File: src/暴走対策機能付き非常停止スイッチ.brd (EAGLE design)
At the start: 14 parts, among them T2 一般的なトランジスタ

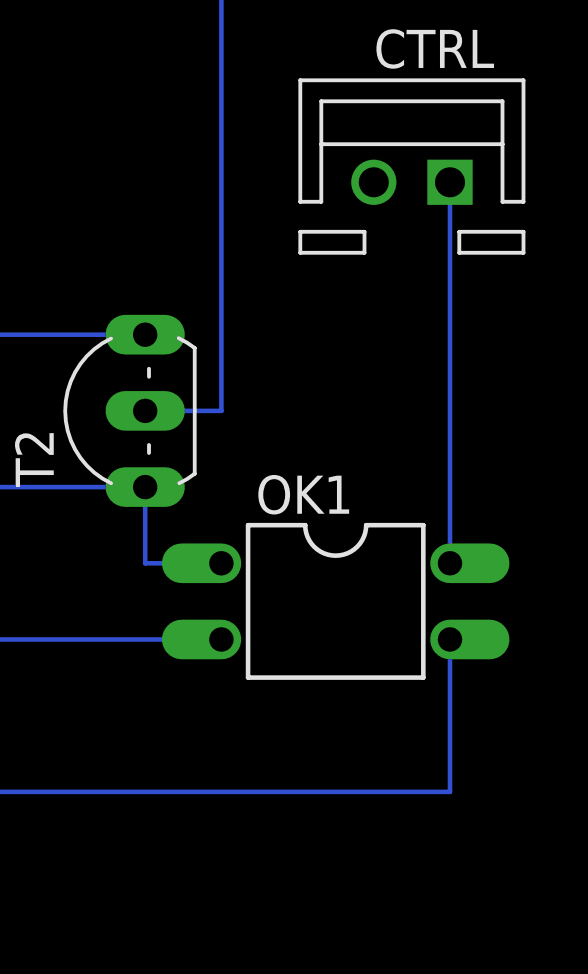
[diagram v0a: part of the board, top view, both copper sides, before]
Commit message: 暴走対策機能付き非常停止スイッチの回路のガバを修復
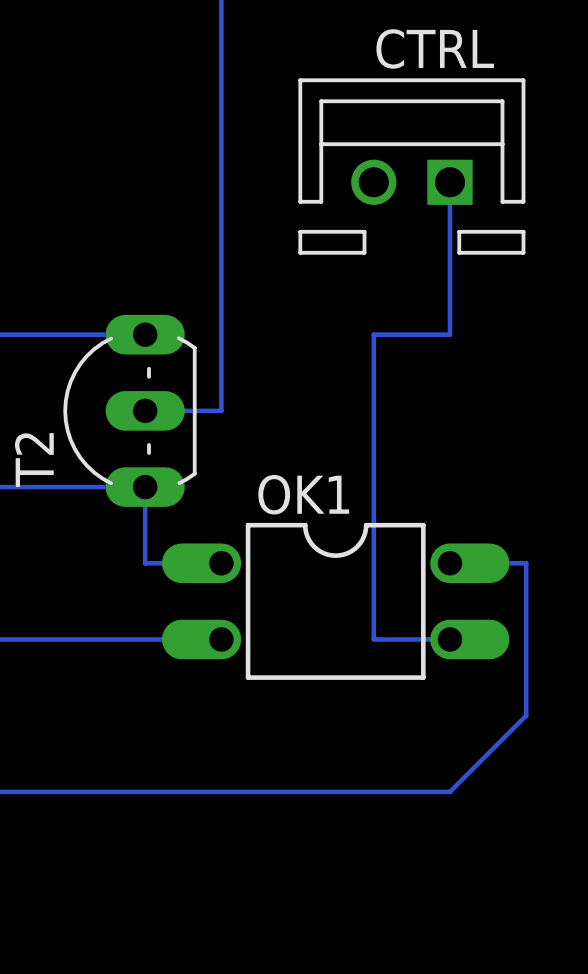
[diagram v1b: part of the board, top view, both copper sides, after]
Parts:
- R5: value 100k -> 10k
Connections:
- net GND2: now also OK1.3; no longer OK1.4
- net N$8: now also OK1.4; no longer OK1.3
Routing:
- net GND2: track 12.7 -> 20.3 mm
- net N$8: track 71.1 -> 77.3 mm
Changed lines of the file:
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@@
 <attribute name="VALUE" x="43.5356" y="20.8026" size="0.9906" layer="27" ratio="10" rot="R180"/>
 </element>
-<element name="R5" library="rcl" library_urn="urn:adsk.eagle:library:334" package="0204/7" package3d_urn="urn:adsk.eagle:package:23498/2" value="100k" x="16.51" y="10.16" smashed="yes">
+<element name="R5" library="rcl" library_urn="urn:adsk.eagle:library:334" package="0204/7" package3d_urn="urn:adsk.eagle:package:23498/2" value="10k" x="16.51" y="10.16" smashed="yes">
 <attribute name="NAME" x="13.97" y="11.4554" size="0.9906" layer="25" ratio="10"/>
 <attribute name="POPULARITY" value="79" x="34.29" y="-29.21" size="1.778" layer="27" display="off"/>
@@
 </signal>
 <signal name="N$8">
-<contactref element="OK1" pad="3"/>
 <contactref element="IRLB-1" pad="G"/>
 <contactref element="R5" pad="1"/>
@@
 <wire x1="12.7" y1="10.16" x2="12.7" y2="15.24" width="0.1524" layer="16"/>
 <wire x1="12.7" y1="15.24" x2="68.58" y2="15.24" width="0.1524" layer="16"/>
-<wire x1="68.58" y1="15.24" x2="68.58" y2="20.32" width="0.1524" layer="16"/>
+<contactref element="OK1" pad="4"/>
+<wire x1="68.58" y1="15.24" x2="71.12" y2="17.78" width="0.1524" layer="16"/>
+<wire x1="71.12" y1="17.78" x2="71.12" y2="22.86" width="0.1524" layer="16"/>
+<wire x1="71.12" y1="22.86" x2="68.58" y2="22.86" width="0.1524" layer="16"/>
 </signal>
 <signal name="INPUT">
@@
 <signal name="GND2">
 <contactref element="CTRL" pad="1"/>
-<contactref element="OK1" pad="4"/>
-<wire x1="68.58" y1="22.86" x2="68.58" y2="35.56" width="0.1524" layer="16"/>
+<contactref element="OK1" pad="3"/>
+<wire x1="68.58" y1="20.32" x2="66.04" y2="20.32" width="0.1524" layer="16"/>
+<wire x1="66.04" y1="20.32" x2="66.04" y2="30.48" width="0.1524" layer="16"/>
+<wire x1="66.04" y1="30.48" x2="68.58" y2="30.48" width="0.1524" layer="16"/>
+<wire x1="68.58" y1="30.48" x2="68.58" y2="35.56" width="0.1524" layer="16"/>
 </signal>
 </signals>
